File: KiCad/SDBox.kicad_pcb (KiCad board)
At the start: 4 copper layers, 52.5 x 59 mm, 23 parts, among them J1 DB25_Male, J2 Micro_SD_Card_Socket, J3 Conn_01x05, U1 Rapberry_Pi_Pico_2W, U2 SN74CBT16210

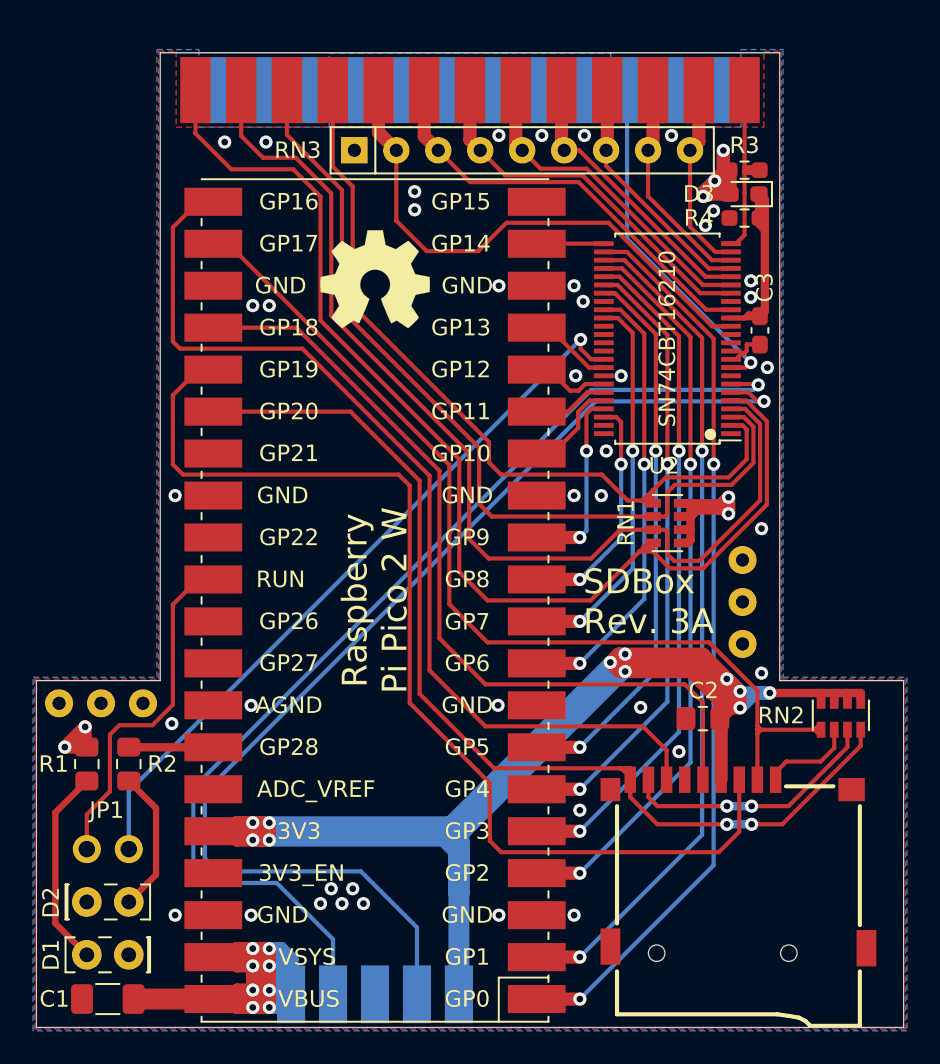
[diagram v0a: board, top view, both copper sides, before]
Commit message: Extended board 1 mm, moved RN3 0.5 mm on Y-axis and changed hole size on JP1, D1, D2 to 0.8 mm, bumped revision to 3B
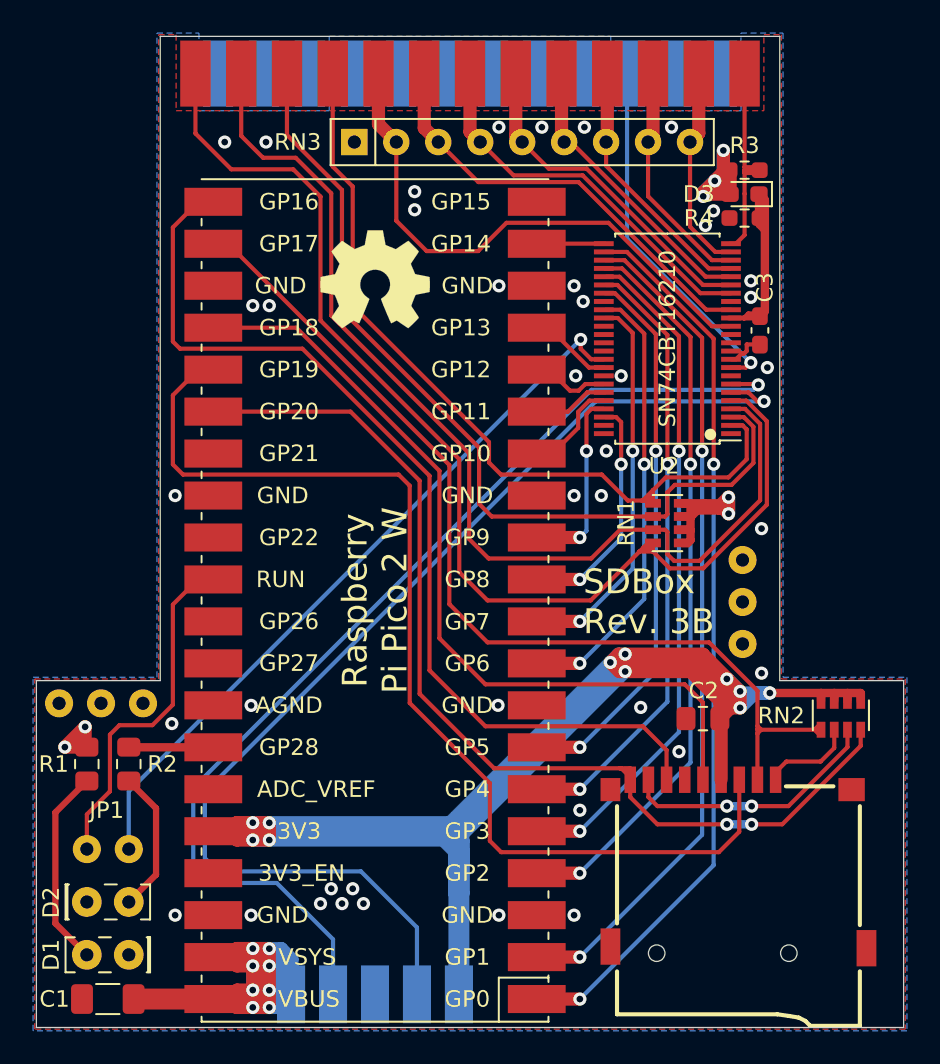
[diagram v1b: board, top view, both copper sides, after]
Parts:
- moved J1 1.00 mm to (147.7, 86.0)
- moved RN3 0.50 mm to (140.7, 90.4)
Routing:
- net RESET: track 21.4 -> 22.6 mm
- net POUT: track 62.8 -> 63.8 mm
- net STROBE: track 12.8 -> 13.8 mm
- net D7: track 32.6 -> 33.6 mm
- net D1: track 13.2 -> 14.2 mm
- net BUSY: track 52.8 -> 53.8 mm
- net ACK: track 49.1 -> 50.1 mm
- net D0: track 11.6 -> 12.6 mm
- net SELECT: track 70.6 -> 71.6 mm
- net D2: track 14.7 -> 15.6 mm
- net D4: track 19.7 -> 20.4 mm
- net D6: track 25.7 -> 26.4 mm
- net D5: track 22.7 -> 23.4 mm
- net D3: track 16.9 -> 17.6 mm
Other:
- board size 52.5 x 59 mm -> 52.5 x 60 mm
- board text added: "SDBox Rev. 3B"
- board text removed: "SDBox Rev. 3A"

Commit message: Change R1 value from 330 to 4.7k, Change R2 value from 330 to 220
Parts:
- R1: value 330 -> 4.7k
- R2: value 330 -> 220
